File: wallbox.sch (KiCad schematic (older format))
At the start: 47 parts, among them J1 From Transformer, J2 To Wallbox, J3 UART, J4 Program, Q1 BC547, Q2 BC547, Q3 BC547, SW1 SW_Push, U1 KA78R33, U2 LM7805CT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

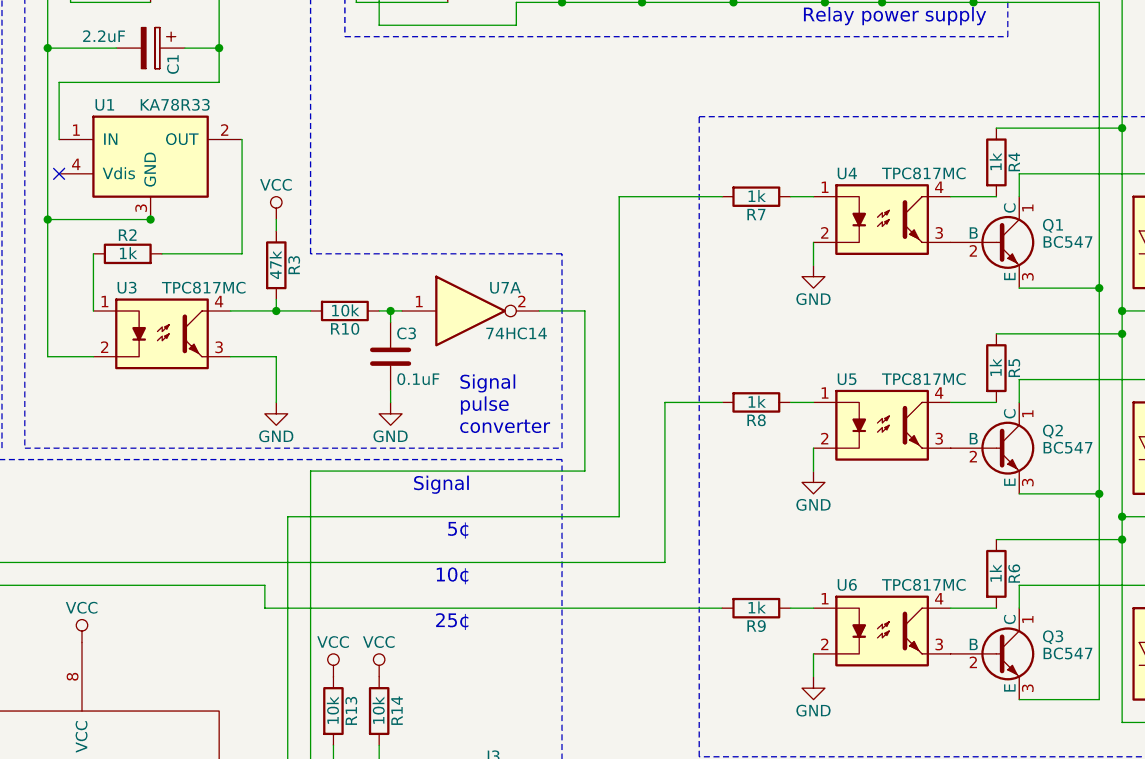
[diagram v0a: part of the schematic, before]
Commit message: Change TPC817 parts from DIP-4M version to DIP-4 version
We could have swapped the footprints, but it makes more sense to just
order the other size part before making another revision. That way we
can save the DIP-4M parts for testing, and can keep the smaller
footprint.
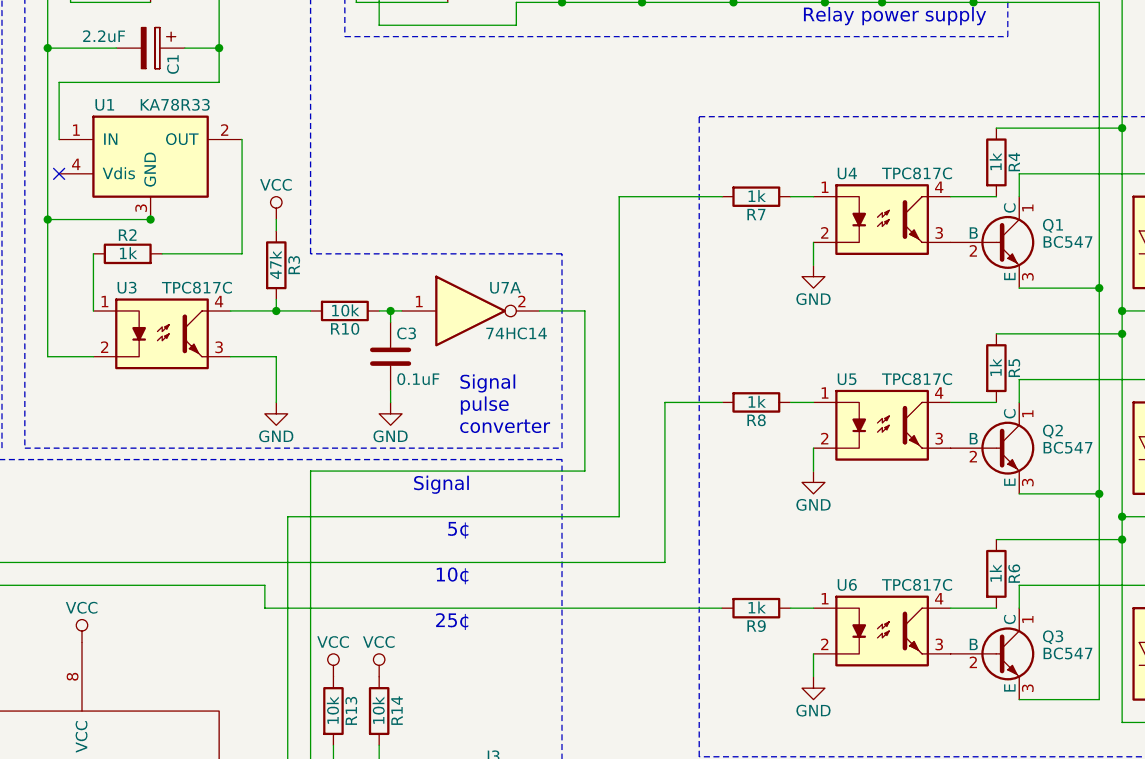
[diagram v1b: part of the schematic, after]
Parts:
- U3, U4, U5, U6: value TPC817MC -> TPC817C; Description OPTOISO 5KV TRANS DIP-4M -> OPTOISO 5KV TRANS DIP-4
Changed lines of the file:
@@
 P 3850 3950
 F 0 "U3" H 3650 4150 50  0000 L CNN
-F 1 "TPC817MC" H 3850 4150 50  0000 L CNN
+F 1 "TPC817C" H 3850 4150 50  0000 L CNN
 F 2 "Housings_DIP:DIP-4_W7.62mm_LongPads" H 3650 3750 50  0001 L CIN
 F 3 "http://www.taiwansemi.com/products/datasheet/TPC817%20SERIES_C1612.pdf" H 3850 3950 50  0001 L CNN
-F 4 "OPTOISO 5KV TRANS DIP-4M" H 3850 3950 60  0001 C CNN "Description"
+F 4 "OPTOISO 5KV TRANS DIP-4" H 3850 3950 60  0001 C CNN "Description"
 	1    3850 3950
 	1    0    0    -1
@@
 P 7000 3450
 F 0 "U4" H 6800 3650 50  0000 L CNN
-F 1 "TPC817MC" H 7000 3650 50  0000 L CNN
+F 1 "TPC817C" H 7000 3650 50  0000 L CNN
 F 2 "Housings_DIP:DIP-4_W7.62mm_LongPads" H 6800 3250 50  0001 L CIN
 F 3 "http://www.taiwansemi.com/products/datasheet/TPC817%20SERIES_C1612.pdf" H 7000 3450 50  0001 L CNN
-F 4 "OPTOISO 5KV TRANS DIP-4M" H 7000 3450 60  0001 C CNN "Description"
+F 4 "OPTOISO 5KV TRANS DIP-4" H 7000 3450 60  0001 C CNN "Description"
 	1    7000 3450
 	1    0    0    -1
@@
 P 7000 4350
 F 0 "U5" H 6800 4550 50  0000 L CNN
-F 1 "TPC817MC" H 7000 4550 50  0000 L CNN
+F 1 "TPC817C" H 7000 4550 50  0000 L CNN
 F 2 "Housings_DIP:DIP-4_W7.62mm_LongPads" H 6800 4150 50  0001 L CIN
 F 3 "http://www.taiwansemi.com/products/datasheet/TPC817%20SERIES_C1612.pdf" H 7000 4350 50  0001 L CNN
-F 4 "OPTOISO 5KV TRANS DIP-4M" H 7000 4350 60  0001 C CNN "Description"
+F 4 "OPTOISO 5KV TRANS DIP-4" H 7000 4350 60  0001 C CNN "Description"
 	1    7000 4350
 	1    0    0    -1
@@
 P 7000 5250
 F 0 "U6" H 6800 5450 50  0000 L CNN
-F 1 "TPC817MC" H 7000 5450 50  0000 L CNN
+F 1 "TPC817C" H 7000 5450 50  0000 L CNN
 F 2 "Housings_DIP:DIP-4_W7.62mm_LongPads" H 6800 5050 50  0001 L CIN
 F 3 "http://www.taiwansemi.com/products/datasheet/TPC817%20SERIES_C1612.pdf" H 7000 5250 50  0001 L CNN
-F 4 "OPTOISO 5KV TRANS DIP-4M" H 7000 5250 60  0001 C CNN "Description"
+F 4 "OPTOISO 5KV TRANS DIP-4" H 7000 5250 60  0001 C CNN "Description"
 	1    7000 5250
 	1    0    0    -1

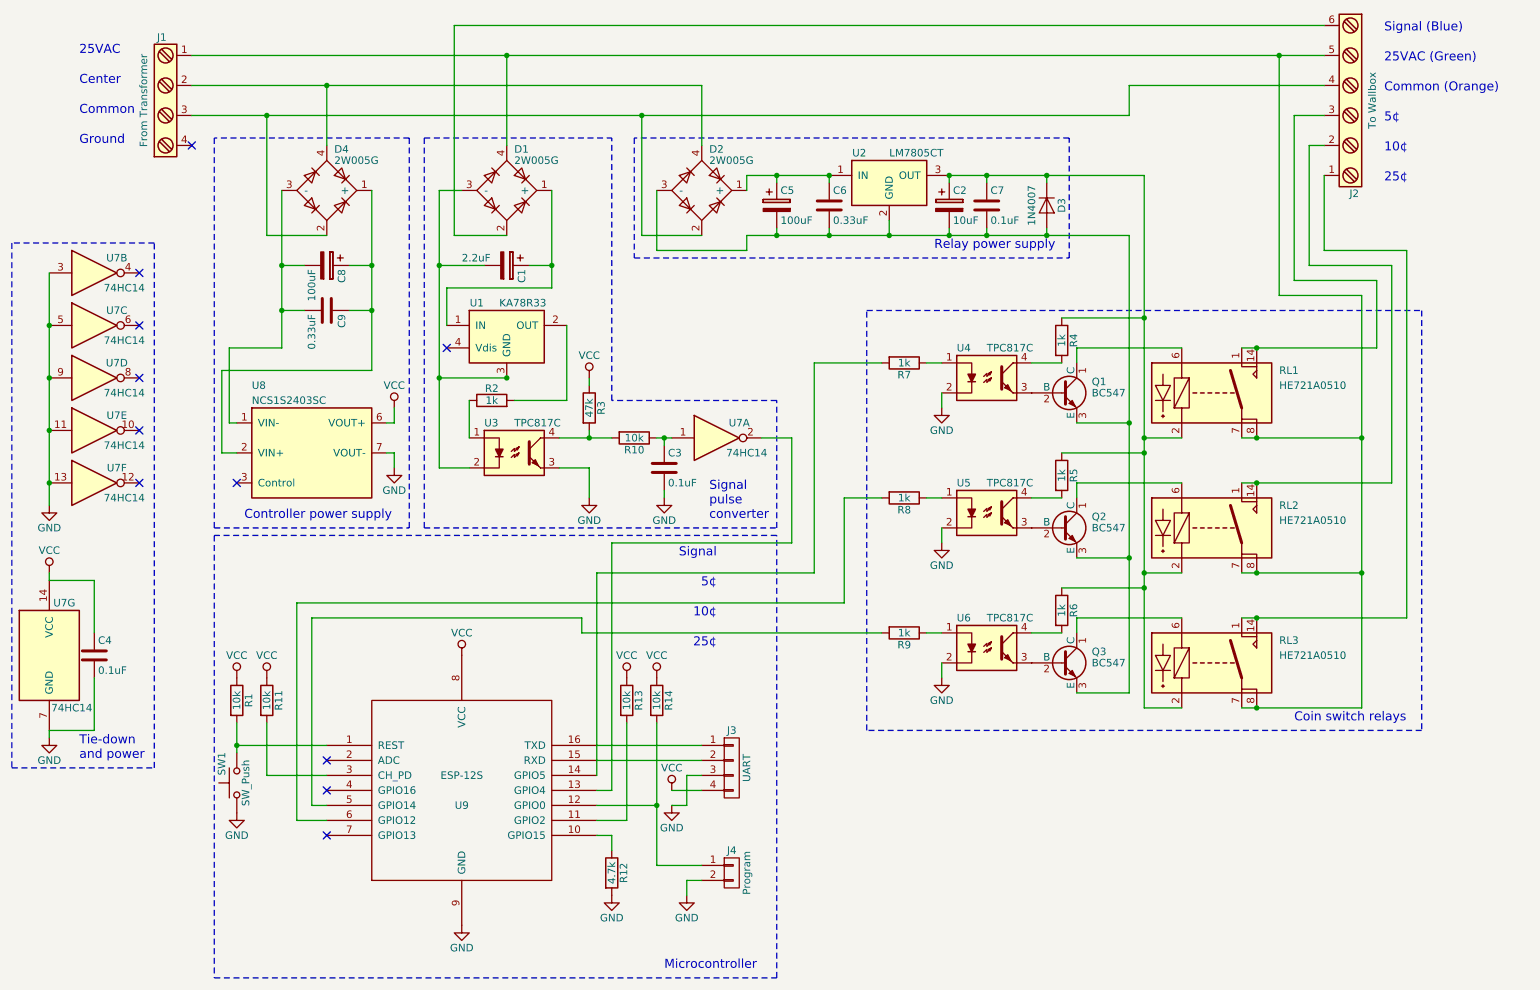
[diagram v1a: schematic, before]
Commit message: Added controller reg caps and config button
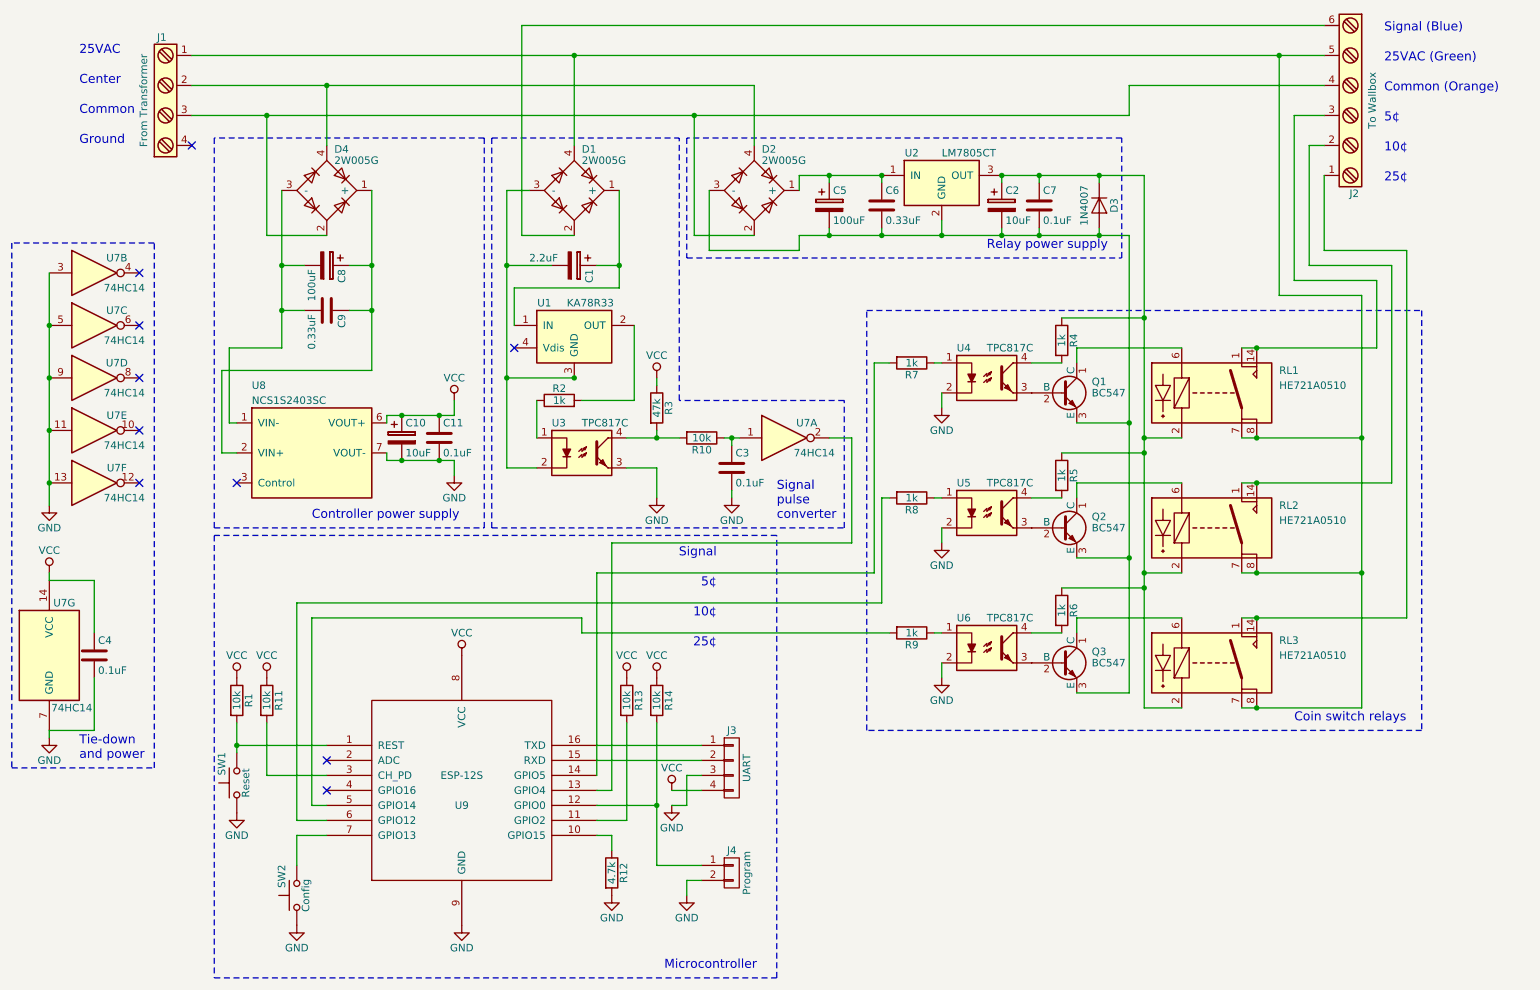
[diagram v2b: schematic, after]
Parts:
- added C10: 10uF, Capacitors_THT:CP_Radial_D5.0mm_P2.00mm, symbol CP
- added C11: 0.1uF, Capacitors_THT:C_Disc_D5.0mm_W2.5mm_P5.00mm, symbol C
- added SW2: Config, Buttons_Switches_THT:SW_PUSH_6mm_h5mm, symbol SW_Push
- SW1: value SW_Push -> Reset
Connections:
- net GND: now also C10.2, C11.2, SW2.1
- net VCC: now also C10.1, C11.1
- net at U9.7 (GPIO13): now also SW2.2
- no-connect marks 11 -> 10
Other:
- moved on the sheet: C1, C2, C3, C5, C6, C7, D1, D2, D3, R10, R2, R3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

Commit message: Moved all the relevant BOM data into KiCAD
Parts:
- C1: Manufacturer (none) -> Nichicon; Manufacturer PN (none) -> UPS1H2R2MDD1TD; Supplier (none) -> Digi-Key; Supplier PN (none) -> 493-5369-1-ND
- C10, C2: Manufacturer (none) -> Nichicon; Manufacturer PN (none) -> UPW1E100MDD1TD; Supplier (none) -> Digi-Key; Supplier PN (none) -> 493-11346-1-ND
- C11, C3, C4, C7: Manufacturer (none) -> Vishay; Manufacturer PN (none) -> K104K15X7RF5TH5; Supplier (none) -> Digi-Key; Supplier PN (none) -> BC1101CT-ND
- C5, C8: Manufacturer (none) -> Nichicon; Manufacturer PN (none) -> UVZ1H101MPD1TD; Supplier (none) -> Digi-Key; Supplier PN (none) -> 493-13464-1-ND
- C6, C9: Manufacturer (none) -> United Chemi-Con; Manufacturer PN (none) -> KVD500L334M32A0T00; Supplier (none) -> Digi-Key; Supplier PN (none) -> 565-4728-1-ND
- D1, D2, D4: Manufacturer (none) -> Vishay; Manufacturer PN (none) -> 2W005G-E4/51; Supplier (none) -> Digi-Key; Supplier PN (none) -> 2W005G-E4/51GI-ND
- D3: Manufacturer (none) -> Micro Commercial; Manufacturer PN (none) -> 1N4007-TP; Supplier (none) -> Digi-Key; Supplier PN (none) -> 1N4007-TPMSCT-ND
- J1: Manufacturer (none) -> Phoenix Contact; Manufacturer PN (none) -> 1729034; Supplier (none) -> Digi-Key; Supplier PN (none) -> 277-1238-ND
- J2: Manufacturer (none) -> Phoenix Contact; Manufacturer PN (none) -> 1729050; Supplier (none) -> Digi-Key; Supplier PN (none) -> 277-1240-ND
- J3: Manufacturer (none) -> Wurth Electronics; Manufacturer PN (none) -> 61300411121; Supplier (none) -> Digi-Key; Supplier PN (none) -> 732-5317-ND
- J4: Manufacturer (none) -> Wurth Electronics; Manufacturer PN (none) -> 61300211121; Supplier (none) -> Digi-Key; Supplier PN (none) -> 732-5315-ND
- Q1, Q2, Q3: Manufacturer (none) -> Fairchild; Manufacturer PN (none) -> BC547BBU; Supplier (none) -> Digi-Key; Supplier PN (none) -> BC547BBU-ND
- R1, R10, R11, R13, R14: Manufacturer (none) -> Stackpole Electronics; Manufacturer PN (none) -> CF14JT10K0; Supplier (none) -> Digi-Key; Supplier PN (none) -> CF14JT10K0CT-ND
- R12: Manufacturer (none) -> Stackpole Electronics; Manufacturer PN (none) -> CF14JT4K70; Supplier (none) -> Digi-Key; Supplier PN (none) -> CF14JT4K70CT-ND
- R2, R4, R5, R6, R7, R8, R9: Manufacturer (none) -> Stackpole Electronics; Manufacturer PN (none) -> CF14JT1K00; Supplier (none) -> Digi-Key; Supplier PN (none) -> CF14JT1K00CT-ND
- R3: Manufacturer (none) -> Stackpole Electronics; Manufacturer PN (none) -> CF14JT47K0; Supplier (none) -> Digi-Key; Supplier PN (none) -> CF14JT47K0CT-ND
- RL1, RL2, RL3: Manufacturer (none) -> Littelfuse; Manufacturer PN (none) -> HE721A0510; Supplier (none) -> Digi-Key; Supplier PN (none) -> HE101-ND
- SW1: Manufacturer (none) -> TE Connectivity; Manufacturer PN (none) -> 1825910-7; Supplier (none) -> Digi-Key; Supplier PN (none) -> 450-1804-ND
- SW2: Manufacturer (none) -> TE Connectivity; Manufacturer PN (none) -> 1825910-6; Supplier (none) -> Digi-Key; Supplier PN (none) -> 450-1650-ND
- U1: Manufacturer (none) -> Fairchild; Manufacturer PN (none) -> KA78R33CTU; Supplier (none) -> Digi-Key; Supplier PN (none) -> KA78R33CTUFS-ND
- U2: Manufacturer (none) -> Fairchild; Manufacturer PN (none) -> LM7805CT; Supplier (none) -> Digi-Key; Supplier PN (none) -> LM7805CT-ND
- U3, U4, U5, U6: Manufacturer (none) -> Taiwan Semiconductor; Manufacturer PN (none) -> TPC817C C9G; Supplier (none) -> Digi-Key; Supplier PN (none) -> TPC817C C9G-ND
- U7: Manufacturer (none) -> Texas Instruments; Manufacturer PN (none) -> SN74HC14N; Supplier (none) -> Digi-Key; Supplier PN (none) -> 296-1577-5-ND
- U8: Manufacturer (none) -> Murata; Manufacturer PN (none) -> NCS1S2403SC; Supplier (none) -> Digi-Key; Supplier PN (none) -> 811-2947-ND
- U9: Manufacturer (none) -> Ai-Thinker; Manufacturer PN (none) -> ESP-12S; Supplier (none) -> Digi-Key; Supplier PN (none) -> 1528-1438-ND
